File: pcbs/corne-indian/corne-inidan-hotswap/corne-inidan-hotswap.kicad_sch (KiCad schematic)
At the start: 0 parts

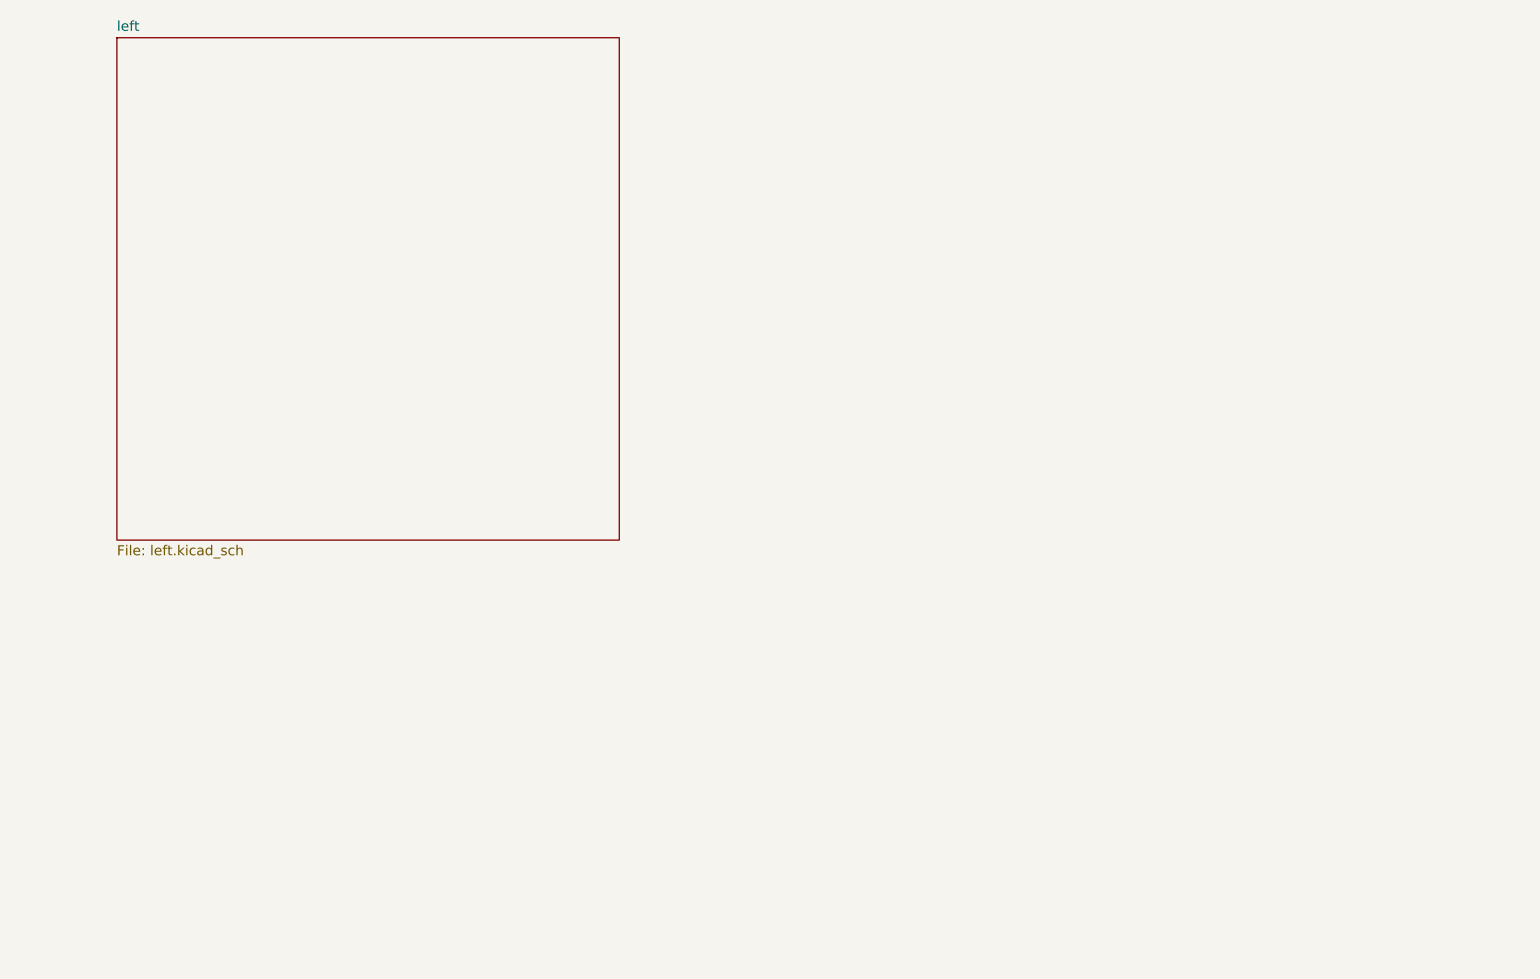
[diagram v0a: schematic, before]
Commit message: Schematic is Done for Right side But Only switch & LED & placement
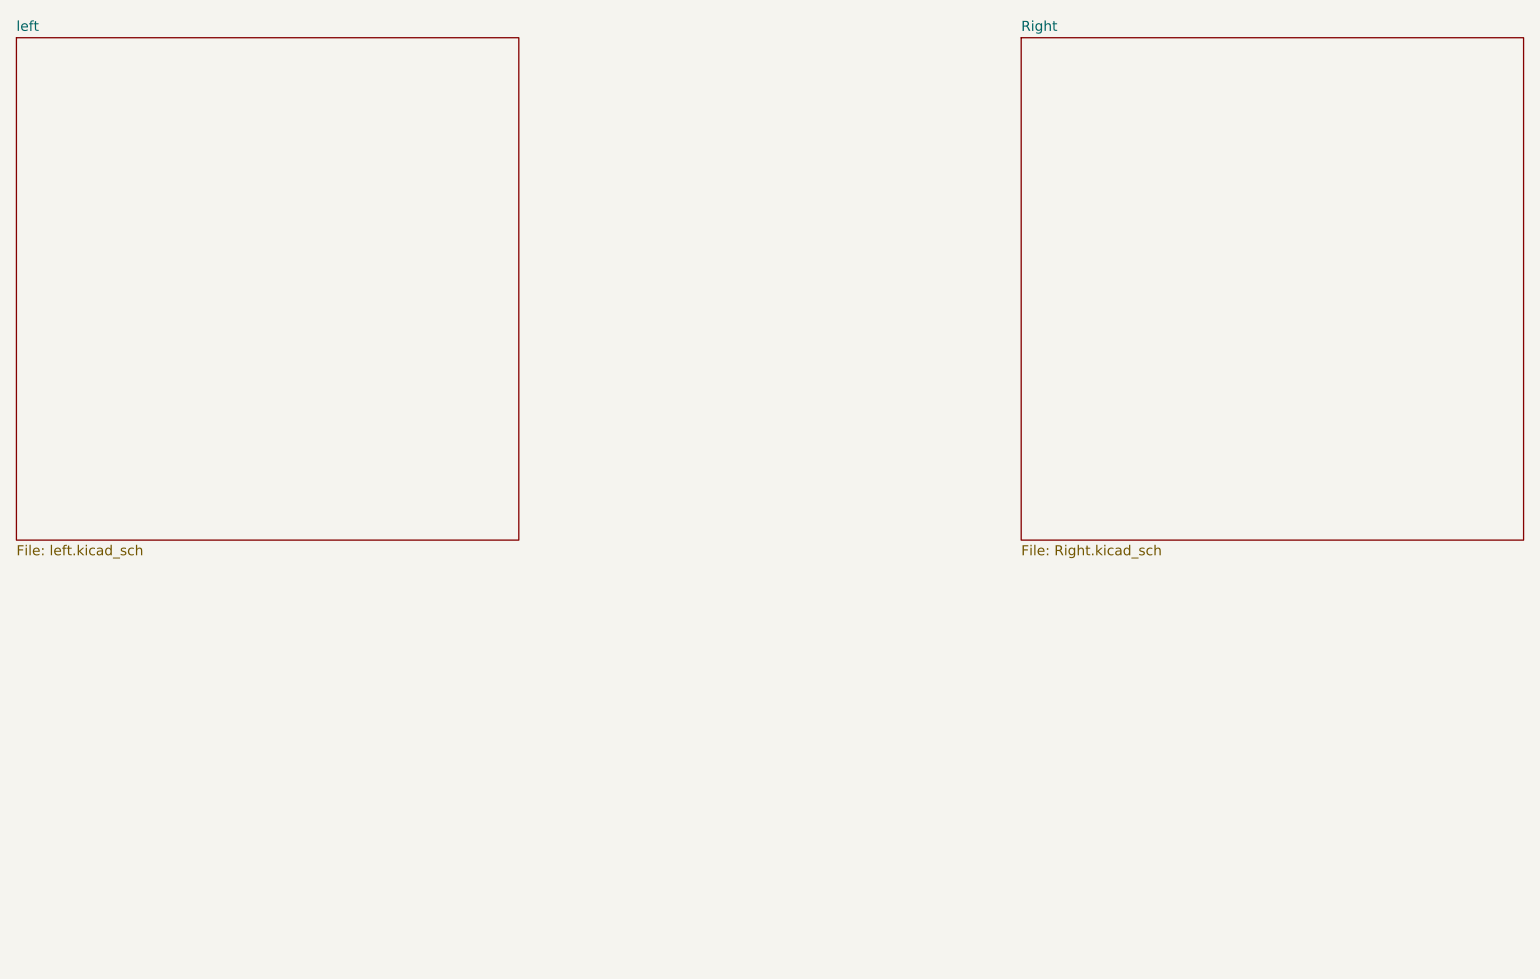
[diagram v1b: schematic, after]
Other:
- added sheet Right (Right.kicad_sch)
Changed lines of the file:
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@@
 	(paper "A4")
 	(sheet
-		(at 50.8 63.5)
+		(at 165.1 63.5)
+		(size 63.5 63.5)
+		(exclude_from_sim no)
+		(in_bom yes)
+		(on_board yes)
+		(dnp no)
+		(fields_autoplaced yes)
+		(stroke
+			(width 0.1524)
+			(type solid)
+		)
+		(fill
+			(color 0 0 0 0.0000)
+		)
+		(property "Sheetname" "Right"
+			(at 165.1 62.7884 0)
+			(effects
+				(font
+					(size 1.27 1.27)
+				)
+				(justify left bottom)
+			)
+		)
+		(property "Sheetfile" "Right.kicad_sch"
+			(at 165.1 127.5846 0)
+			(effects
+				(font
+					(size 1.27 1.27)
+				)
+				(justify left top)
+			)
+		)
+		(instances
+			(project "corne-inidan-hotswap"
+				(path "/c90c0725-f1d3-4c5d-9757-c1f2f2a5449f"
+					(page "4")
+				)
+			)
+		)
+	)
+	(sheet
+		(at 38.1 63.5)
 		(size 63.5 63.5)
 		(exclude_from_sim no)
@@
 		)
 		(property "Sheetname" "left"
-			(at 50.8 62.7884 0)
+			(at 38.1 62.7884 0)
 			(effects
 				(font
@@
 		)
 		(property "Sheetfile" "left.kicad_sch"
-			(at 50.8 127.5846 0)
+			(at 38.1 127.5846 0)
 			(effects
 				(font

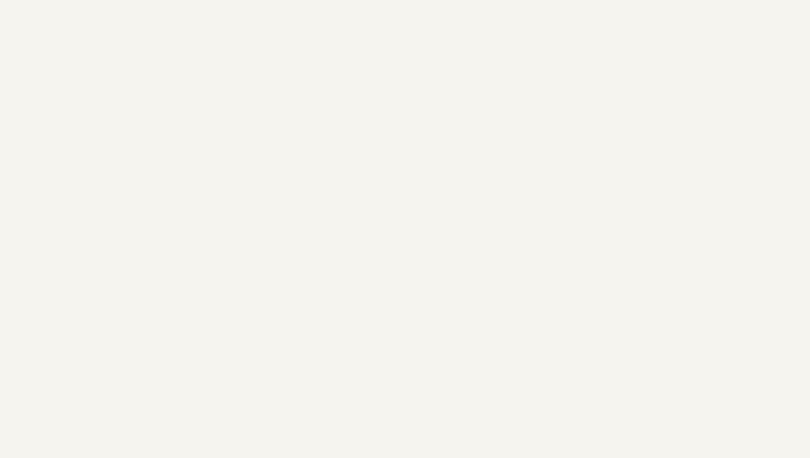
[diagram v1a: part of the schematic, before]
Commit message: Mid of the Component placement still the Rotarty nob is not done
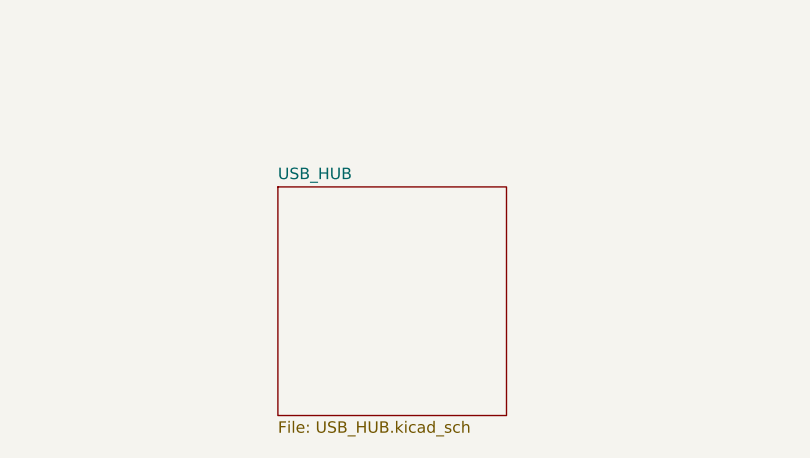
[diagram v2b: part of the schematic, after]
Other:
- added sheet USB_HUB (USB_HUB.kicad_sch)
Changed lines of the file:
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@@
+			(project "corne-inidan-hotswap"
+				(path "/c90c0725-f1d3-4c5d-9757-c1f2f2a5449f"
+					(page "3")
+				)
+			)
+		)
+	)
+	(sheet
+		(at 114.3 152.4)
+		(size 25.4 25.4)
+		(exclude_from_sim no)
+		(in_bom yes)
+		(on_board yes)
+		(dnp no)
+		(fields_autoplaced yes)
+		(stroke
+			(width 0.1524)
+			(type solid)
+		)
+		(fill
+			(color 0 0 0 0.0000)
+		)
+		(property "Sheetname" "USB_HUB"
+			(at 114.3 151.6884 0)
+			(effects
+				(font
+					(size 1.27 1.27)
+				)
+				(justify left bottom)
+			)
+		)
+		(property "Sheetfile" "USB_HUB.kicad_sch"
+			(at 114.3 178.3846 0)
+			(effects
+				(font
+					(size 1.27 1.27)
+				)
+				(justify left top)
+			)
+		)
+		(instances
 			(project "corne-inidan-hotswap"
 				(path "/c90c0725-f1d3-4c5d-9757-c1f2f2a5449f"

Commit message: Double check with corne is also schematic apart from esd diode reset is done
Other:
- removed sheet USB_HUB
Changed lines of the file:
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@@
-	)
-	(sheet
-		(at 114.3 152.4)
-		(size 25.4 25.4)
-		(exclude_from_sim no)
-		(in_bom yes)
-		(on_board yes)
-		(dnp no)
-		(fields_autoplaced yes)
-		(stroke
-			(width 0.1524)
-			(type solid)
-		)
-		(fill
-			(color 0 0 0 0.0000)
-		)
-		(property "Sheetname" "USB_HUB"
-			(at 114.3 151.6884 0)
-			(effects
-				(font
-					(size 1.27 1.27)
-				)
-				(justify left bottom)
-			)
-		)
-		(property "Sheetfile" "USB_HUB.kicad_sch"
-			(at 114.3 178.3846 0)
-			(effects
-				(font
-					(size 1.27 1.27)
-				)
-				(justify left top)
-			)
-		)
-		(instances
-			(project "corne-inidan-hotswap"
-				(path "/c90c0725-f1d3-4c5d-9757-c1f2f2a5449f"
-					(page "4")
-				)
-			)
-		)
 	)
 	(sheet
